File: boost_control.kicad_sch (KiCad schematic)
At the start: 5 parts, among them U2 AD5259BRMZ100

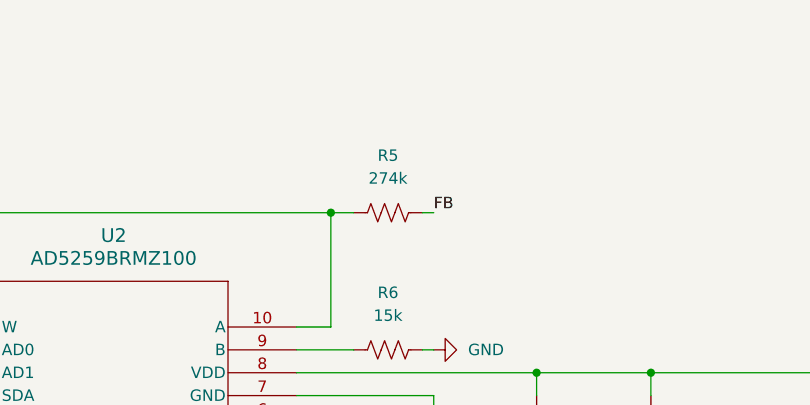
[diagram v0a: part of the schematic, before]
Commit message: Eiditng frontend
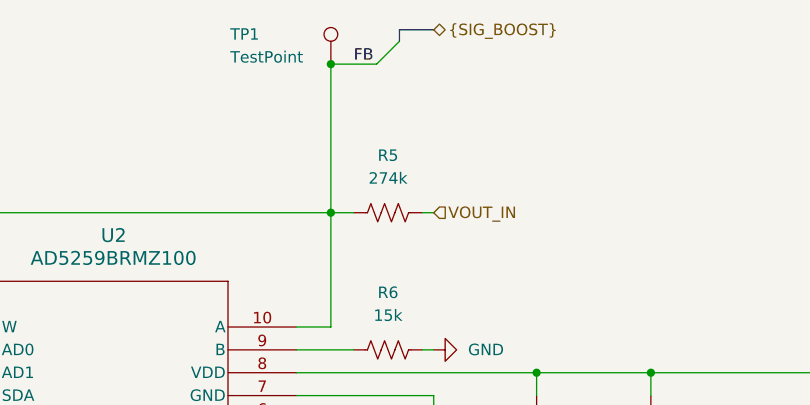
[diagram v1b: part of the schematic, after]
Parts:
- added TP1: TestPoint, symbol Connector:TestPoint
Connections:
- net FB: now also R5.1, U2.1 (W), U2.10 (A), TP1.1; no longer R5.2
- new net VOUT_IN: R5.2
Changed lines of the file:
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@@
+	)
+	(junction
+		(at 177.8 60.96)
+		(diameter 0)
+		(color 0 0 0 0)
 	)
 	(junction
@@
 	)
 	(bus_entry
+		(at 185.42 58.42)
+		(size -2.54 2.54)
+		(stroke
+			(width 0)
+			(type default)
+		)
+	)
+	(bus_entry
 		(at 125.73 100.33)
 		(size 2.54 -2.54)
@@
 		)
 	)
+	(wire
+		(pts
+			(xy 177.8 60.96) (xy 182.88 60.96)
+		)
+		(stroke
+			(width 0)
+			(type default)
+		)
+	)
 	(bus
 		(pts
@@
 		)
 	)
+	(bus
+		(pts
+			(xy 185.42 57.15) (xy 189.23 57.15)
+		)
+		(stroke
+			(width 0)
+			(type default)
+		)
+	)
 	(wire
 		(pts
@@
 		)
 	)
+	(bus
+		(pts
+			(xy 185.42 57.15) (xy 185.42 58.42)
+		)
+		(stroke
+			(width 0)
+			(type default)
+		)
+	)
 	(wire
 		(pts
@@
 		(pts
 			(xy 173.99 90.17) (xy 177.8 90.17)
+		)
+		(stroke
+			(width 0)
+			(type default)
+		)
+	)
+	(wire
+		(pts
+			(xy 177.8 77.47) (xy 177.8 60.96)
 		)
 		(stroke
@@
 	)
 	(label "FB"
+		(at 180.34 60.96 0)
+		(effects
+			(font
+				(size 1.27 1.27)
+			)
+			(justify left bottom)
+		)
+	)
+	(hierarchical_label "VOUT_IN"
+		(shape input)
 		(at 189.23 77.47 0)
 		(effects
@@
 				(size 1.27 1.27)
 			)
-			(justify left bottom)
+			(justify left)
 		)
 	)
@@
 			)
 			(justify right)
+		)
+	)
+	(hierarchical_label "{SIG_BOOST}"
+		(shape bidirectional)
+		(at 189.23 57.15 0)
+		(effects
+			(font
+				(size 1.27 1.27)
+			)
+			(justify left)
 		)
 	)
@@
 					(unit 1)
 				)
+			)
+		)
+	)
+	(symbol
+		(lib_id "Connector:TestPoint")
+		(at 177.8 60.96 0)
+		(unit 1)
+		(exclude_from_sim no)
+		(in_bom yes)
+		(on_board yes)
+		(dnp no)
+		(property "Reference" "TP1"
+			(at 166.624 57.658 0)
+			(effects
+				(font
+					(size 1.27 1.27)
+				)
+				(justify left)
+			)
+		)
+		(property "Value" "TestPoint"
+			(at 166.624 60.198 0)
+			(effects
+				(font
+					(size 1.27 1.27)
+				)
+				(justify left)
+			)
+		)
+		(property "Footprint" ""
+			(at 182.88 60.96 0)
+			(effects
+				(font
+					(size 1.27 1.27)
+				)
+				(hide yes)
+			)
+		)
+		(property "Datasheet" "~"
+			(at 182.88 60.96 0)
+			(effects
+				(font
+					(size 1.27 1.27)
+				)
+				(hide yes)
+			)
+		)
+		(property "Description" "test point"
+			(at 177.8 60.96 0)
+			(effects
+				(font
+					(size 1.27 1.27)
+				)
+				(hide yes)
+			)
+		)
+		(pin "1"
+		)
+		(instances
+			(project ""
+				(path "/99785679-20de-4827-b4cc-bc3c187068c9/9564929a-642e-4163-88c2-45054b63a5ed/09b4163a-819e-413e-b808-030375832f4a"
+					(reference "TP1")
+					(unit 1)
+				)
+				(path "/99785679-20de-4827-b4cc-bc3c187068c9/9564929a-642e-4163-88c2-45054b63a5ed/84126d6b-9224-455f-9cea-3582a8eebe20"
+					(reference "TP2")
+					(unit 1)
+				)

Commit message: Working on schematic and layout
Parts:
- TP1: footprint (none) -> TestPoint:TestPoint_Keystone_5015_Micro_Mini
- renumbered C17 to C18, C18 to C19
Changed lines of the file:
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@@
 				)
 				(path "/99785679-20de-4827-b4cc-bc3c187068c9/9564929a-642e-4163-88c2-45054b63a5ed/84126d6b-9224-455f-9cea-3582a8eebe20"
-					(reference "U6")
+					(reference "U7")
 					(unit 1)
 				)
@@
 		(on_board yes)
 		(dnp no)
-		(property "Reference" "C18"
+		(property "Reference" "C19"
 			(at 215.9 100.584 0)
 			(effects
@@
 			(project "PowerBoard"
 				(path "/99785679-20de-4827-b4cc-bc3c187068c9/9564929a-642e-4163-88c2-45054b63a5ed/09b4163a-819e-413e-b808-030375832f4a"
-					(reference "C18")
+					(reference "C19")
 					(unit 1)
 				)
 				(path "/99785679-20de-4827-b4cc-bc3c187068c9/9564929a-642e-4163-88c2-45054b63a5ed/84126d6b-9224-455f-9cea-3582a8eebe20"
-					(reference "C53")
+					(reference "C55")
 					(unit 1)
 				)
@@
 				)
 				(path "/99785679-20de-4827-b4cc-bc3c187068c9/9564929a-642e-4163-88c2-45054b63a5ed/84126d6b-9224-455f-9cea-3582a8eebe20"
-					(reference "R21")
+					(reference "R22")
 					(unit 1)
 				)
@@
 			)
 		)
-		(property "Footprint" ""
+		(property "Footprint" "TestPoint:TestPoint_Keystone_5015_Micro_Mini"
 			(at 182.88 60.96 0)
 			(effects
@@
 		)
 		(property "Description" "test point"
+			(at 177.8 60.96 0)
+			(effects
+				(font
+					(size 1.27 1.27)
+				)
+				(hide yes)
+			)
+		)
+		(property "Mfr" ""
+			(at 177.8 60.96 0)
+			(effects
+				(font
+					(size 1.27 1.27)
+				)
+				(hide yes)
+			)
+		)
+		(property "Mfr P/N" ""
+			(at 177.8 60.96 0)
+			(effects
+				(font
+					(size 1.27 1.27)
+				)
+				(hide yes)
+			)
+		)
+		(property "Supplier_1" ""
+			(at 177.8 60.96 0)
+			(effects
+				(font
+					(size 1.27 1.27)
+				)
+				(hide yes)
+			)
+		)
+		(property "Supplier_1 P/N" ""
+			(at 177.8 60.96 0)
+			(effects
+				(font
+					(size 1.27 1.27)
+				)
+				(hide yes)
+			)
+		)
+		(property "Supplier_1 Unit Price" ""
+			(at 177.8 60.96 0)
+			(effects
+				(font
+					(size 1.27 1.27)
+				)
+				(hide yes)
+			)
+		)
+		(property "Supplier_1 Price @ Qty" ""
+			(at 177.8 60.96 0)
+			(effects
+				(font
+					(size 1.27 1.27)
+				)
+				(hide yes)
+			)
+		)
+		(property "Supplier_2" ""
+			(at 177.8 60.96 0)
+			(effects
+				(font
+					(size 1.27 1.27)
+				)
+				(hide yes)
+			)
+		)
+		(property "Supplier_2 P/N" ""
+			(at 177.8 60.96 0)
+			(effects
+				(font
+					(size 1.27 1.27)
+				)
+				(hide yes)
+			)
+		)
+		(property "Supplier_2 Unit Price" ""
+			(at 177.8 60.96 0)
+			(effects
+				(font
+					(size 1.27 1.27)
+				)
+				(hide yes)
+			)
+		)
+		(property "Supplier_2 Price @ Qty" ""
 			(at 177.8 60.96 0)
 			(effects
@@
 				)
 				(path "/99785679-20de-4827-b4cc-bc3c187068c9/9564929a-642e-4163-88c2-45054b63a5ed/84126d6b-9224-455f-9cea-3582a8eebe20"
-					(reference "R22")
+					(reference "R23")
 					(unit 1)
 				)
@@
 		(on_board yes)
 		(dnp no)
-		(property "Reference" "C17"
+		(property "Reference" "C18"
 			(at 205.232 100.584 0)
 			(effects
@@
 			(project "PowerBoard"
 				(path "/99785679-20de-4827-b4cc-bc3c187068c9/9564929a-642e-4163-88c2-45054b63a5ed/09b4163a-819e-413e-b808-030375832f4a"
-					(reference "C17")
+					(reference "C18")
 					(unit 1)
 				)
 				(path "/99785679-20de-4827-b4cc-bc3c187068c9/9564929a-642e-4163-88c2-45054b63a5ed/84126d6b-9224-455f-9cea-3582a8eebe20"
-					(reference "C52")
-					(unit 1)
-				)
+					(reference "C54")
+					(unit 1)
+				)

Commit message: Pushing
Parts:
- added JP1: SolderJumper_2_Open, Jumper:SolderJumper-2_P1.3mm_Open_RoundedPad1.0x1.5mm, symbol Jumper:SolderJumper_2_Open
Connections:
- net +5V: no longer U2.6 (VLOGIC)
- net FB: now also JP1.1 (A); no longer U2.10 (A)
- net I2C_SETTING: now reaches U2.3 (AD1)
- new net: JP1.2 (B), U2.10 (A)
- new net +3V3: U2.6 (VLOGIC)
- no-connect marks 2 -> 1
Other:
- moved on the sheet: C18, C19, R5, R6, TP1, U2

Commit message: BOM in folder
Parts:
- C18: JLCPCB Status (none) -> JLC in-stock package match; Mfr P/N 06035C104K4T2A -> CC0603KRX7R9BB104; Supplier_1 Digikey -> LCSC; Supplier_1 P/N 478-KAM15AR71H104KTTR-ND -> C14663; Supplier_1 Unit Price 0.10000 -> (none)
- C19: Supplier_1 Digikey -> LCSC; Supplier_1 P/N 490-18663-2-ND -> C440198; Supplier_1 Unit Price 0.28000 -> (none)
- R5: JLCPCB Status (none) -> Similar JLC in-stock package match; Mfr P/N ERA-3AEB2743V -> FRC0603F2743TS; Supplier_1 Digikey -> LCSC; Supplier_1 P/N P274KDBTR-ND -> C5126128; Supplier_1 Unit Price 0.10000 -> (none)
- R6: JLCPCB Status (none) -> JLC in-stock package match; Mfr P/N ERA-3AEB153V -> 0603WAF1502T5E; Supplier_1 Digikey -> LCSC; Supplier_1 P/N P15KDBTR-ND -> C22809; Supplier_1 Unit Price 0.10000 -> (none)
- U2: Supplier_1 Digikey -> LCSC; Supplier_1 P/N AD5259BRMZ100-R7TR-ND -> C141953; Supplier_1 Unit Price 4.45000 -> (none)
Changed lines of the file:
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@@
 			)
 		)
-		(property "Supplier_1" "Digikey"
+		(property "Supplier_1" "LCSC"
 			(at 118.11 93.98 0)
 			(effects
@@
 			)
 		)
-		(property "Supplier_1 P/N" "AD5259BRMZ100-R7TR-ND"
+		(property "Supplier_1 P/N" "C141953"
 			(at 118.11 93.98 0)
 			(effects
@@
 			)
 		)
-		(property "Supplier_1 Unit Price" "4.45000"
+		(property "Supplier_1 Unit Price" ""
 			(at 118.11 93.98 0)
 			(effects
@@
 		)
 		(property "Supplier_2 Price @ Qty" "1"
+			(at 118.11 93.98 0)
+			(effects
+				(font
+					(size 1.27 1.27)
+				)
+				(hide yes)
+			)
+		)
+		(property "SNAPEDA_PN" ""
 			(at 118.11 93.98 0)
 			(effects
@@
 			)
 		)
-		(property "Supplier_1" "Digikey"
+		(property "Supplier_1" "LCSC"
 			(at 198.12 105.41 0)
 			(effects
@@
 			)
 		)
-		(property "Supplier_1 P/N" "490-18663-2-ND"
+		(property "Supplier_1 P/N" "C440198"
 			(at 198.12 105.41 0)
 			(effects
@@
 			)
 		)
-		(property "Supplier_1 Unit Price" "0.28000"
+		(property "Supplier_1 Unit Price" ""
 			(at 198.12 105.41 0)
 			(effects
@@
 		)
 		(property "Supplier_2 Price @ Qty" ""
+			(at 198.12 105.41 0)
+			(effects
+				(font
+					(size 1.27 1.27)
+				)
+				(hide yes)
+			)
+		)
+		(property "SNAPEDA_PN" ""
 			(at 198.12 105.41 0)
 			(effects
@@
 			)
 		)
-		(property "Mfr P/N" "ERA-3AEB2743V"
+		(property "Mfr P/N" "FRC0603F2743TS"
 			(at 168.91 81.28 0)
 			(effects
@@
 			)
 		)
-		(property "Supplier_1" "Digikey"
+		(property "Supplier_1" "LCSC"
 			(at 168.91 81.28 0)
 			(effects
@@
 			)
 		)
-		(property "Supplier_1 P/N" "P274KDBTR-ND"
+		(property "Supplier_1 P/N" "C5126128"
 			(at 168.91 81.28 0)
 			(effects
@@
 			)
 		)
-		(property "Supplier_1 Unit Price" "0.10000"
+		(property "Supplier_1 Unit Price" ""
 			(at 168.91 81.28 0)
 			(effects
@@
 		(property "Supplier_2 Price @ Qty" ""
 			(at 168.91 81.28 0)
+			(effects
+				(font
+					(size 1.27 1.27)
+				)
+				(hide yes)
+			)
+		)
+		(property "JLCPCB Status" "Similar JLC in-stock package match"
+			(at 168.91 81.28 90)
+			(effects
+				(font
+					(size 1.27 1.27)
+				)
+				(hide yes)
+			)
+		)
+		(property "SNAPEDA_PN" ""
+			(at 168.91 81.28 90)
 			(effects
 				(font
@@
 			)
 		)
+		(property "SNAPEDA_PN" ""
+			(at 162.56 64.77 0)
+			(effects
+				(font
+					(size 1.27 1.27)
+				)
+				(hide yes)
+			)
+		)
 		(pin "1"
 		)
@@
 			)
 		)
-		(property "Mfr P/N" "ERA-3AEB153V"
+		(property "Mfr P/N" "0603WAF1502T5E"
 			(at 168.91 96.52 0)
 			(effects
@@
 			)
 		)
-		(property "Supplier_1" "Digikey"
+		(property "Supplier_1" "LCSC"
 			(at 168.91 96.52 0)
 			(effects
@@
 			)
 		)
-		(property "Supplier_1 P/N" "P15KDBTR-ND"
+		(property "Supplier_1 P/N" "C22809"
 			(at 168.91 96.52 0)
 			(effects
@@
 			)
 		)
-		(property "Supplier_1 Unit Price" "0.10000"
+		(property "Supplier_1 Unit Price" ""
 			(at 168.91 96.52 0)
 			(effects
@@
 		(property "Supplier_2 Price @ Qty" ""
 			(at 168.91 96.52 0)
+			(effects
+				(font
+					(size 1.27 1.27)
+				)
+				(hide yes)
+			)
+		)
+		(property "JLCPCB Status" "JLC in-stock package match"
+			(at 168.91 96.52 90)
+			(effects
+				(font
+					(size 1.27 1.27)
+				)
+				(hide yes)
+			)
+		)
+		(property "SNAPEDA_PN" ""
+			(at 168.91 96.52 90)
 			(effects
 				(font
@@
 			)
 		)
+		(property "SNAPEDA_PN" ""
+			(at 162.56 87.63 90)
+			(effects
+				(font
+					(size 1.27 1.27)
+				)
+				(hide yes)
+			)
+		)
 		(pin "1"
 		)
@@
 			)
 		)
-		(property "Mfr P/N" "06035C104K4T2A"
+		(property "Mfr P/N" "CC0603KRX7R9BB104"
 			(at 185.42 105.41 0)
 			(effects
@@
 			)
 		)
-		(property "Supplier_1" "Digikey"
+		(property "Supplier_1" "LCSC"
 			(at 185.42 105.41 0)
 			(effects
@@
 			)
 		)
-		(property "Supplier_1 P/N" "478-KAM15AR71H104KTTR-ND"
+		(property "Supplier_1 P/N" "C14663"
 			(at 185.42 105.41 0)
 			(effects
@@
 			)
 		)
-		(property "Supplier_1 Unit Price" "0.10000"
+		(property "Supplier_1 Unit Price" ""
 			(at 185.42 105.41 0)
 			(effects
@@
 			(at 185.42 105.41 0)
 			(effects
+				(font
+					(size 1.27 1.27)
+				)
+				(hide yes)
+			)
+		)
+		(property "JLCPCB Status" "JLC in-stock package match"
+			(at 185.42 105.41 0)
+			(effects
+				(font
+					(size 1.27 1.27)
+				)
+				(hide yes)
+			)
+		)
+		(property "SNAPEDA_PN" ""
+			(at 185.42 105.41 0)
+			(effects

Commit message: Schematic updates
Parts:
- U2: Supplier_1 Price @ Qty 1 -> (none); Supplier_2 Analog Devices -> (none); Supplier_2 P/N C141953 -> (none); Supplier_2 Price @ Qty 1 -> (none); Supplier_2 Unit Price 3.2689 -> (none)
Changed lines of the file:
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@@
 			)
 		)
-		(property "Supplier_1 Price @ Qty" "1"
+		(property "Supplier_1 Price @ Qty" ""
 			(at 118.11 93.98 0)
 			(effects
@@
 			)
 		)
-		(property "Supplier_2" "Analog Devices"
+		(property "Supplier_2" ""
 			(at 118.11 93.98 0)
 			(effects
@@
 			)
 		)
-		(property "Supplier_2 P/N" "C141953"
+		(property "Supplier_2 P/N" ""
 			(at 118.11 93.98 0)
 			(effects
@@
 			)
 		)
-		(property "Supplier_2 Unit Price" "3.2689"
+		(property "Supplier_2 Unit Price" ""
 			(at 118.11 93.98 0)
 			(effects
@@
 			)
 		)
-		(property "Supplier_2 Price @ Qty" "1"
+		(property "Supplier_2 Price @ Qty" ""
 			(at 118.11 93.98 0)
 			(effects

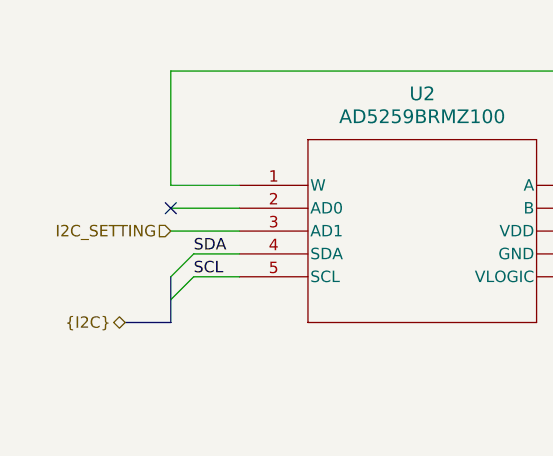
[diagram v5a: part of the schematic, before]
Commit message: i2c 0 and 1 bus routed + mosfet logic change
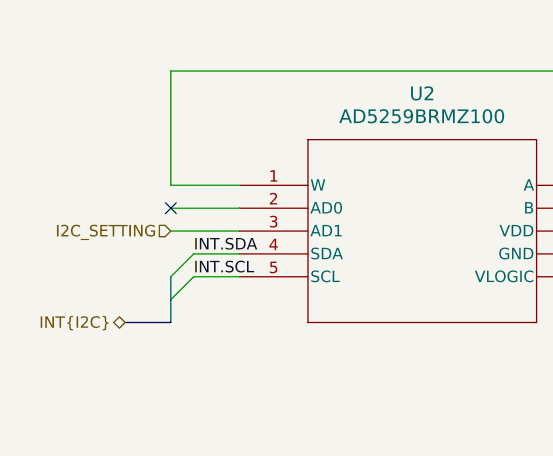
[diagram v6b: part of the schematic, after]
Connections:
- net SCL renamed INT.SCL
- net SDA renamed INT.SDA
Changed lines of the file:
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@@
+		)
+	)
+	(bus
+		(pts
+			(xy 110.49 104.14) (xy 110.49 106.68)
+		)
+		(stroke
+			(width 0)
+			(type default)
 		)
 	)
@@
 		)
 	)
-	(bus
-		(pts
-			(xy 110.49 104.14) (xy 110.49 106.68)
-		)
-		(stroke
-			(width 0)
-			(type default)
-		)
-	)
 	(wire
 		(pts
@@
 		)
 	)
+	(bus
+		(pts
+			(xy 105.41 109.22) (xy 110.49 109.22)
+		)
+		(stroke
+			(width 0)
+			(type default)
+		)
+	)
 	(wire
 		(pts
@@
 		)
 	)
-	(bus
-		(pts
-			(xy 105.41 109.22) (xy 110.49 109.22)
-		)
-		(stroke
-			(width 0)
-			(type default)
-		)
-	)
 	(wire
 		(pts
@@
 		)
 	)
-	(label "SDA"
+	(label "INT.SDA"
 		(at 113.03 101.6 0)
 		(effects
@@
 		)
 	)
-	(label "SCL"
+	(label "INT.SCL"
 		(at 113.03 104.14 0)
 		(effects
@@
 		)
 	)
-	(hierarchical_label "{I2C}"
+	(hierarchical_label "INT{I2C}"
 		(shape bidirectional)
 		(at 105.41 109.22 180)
